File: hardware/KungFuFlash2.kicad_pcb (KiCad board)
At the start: 2 copper layers, 60.6 x 62 mm, 53 parts, among them J1 SWD, J2 USB_B_Micro, J3 Wifi, Q1 BC817, SW1 Reset, SW2 Menu, SW3 Special, U1 C64-Exp-Port, U2 AMS1117-3.3, U3 STM32H7B0VBTx, Y1 25MHz

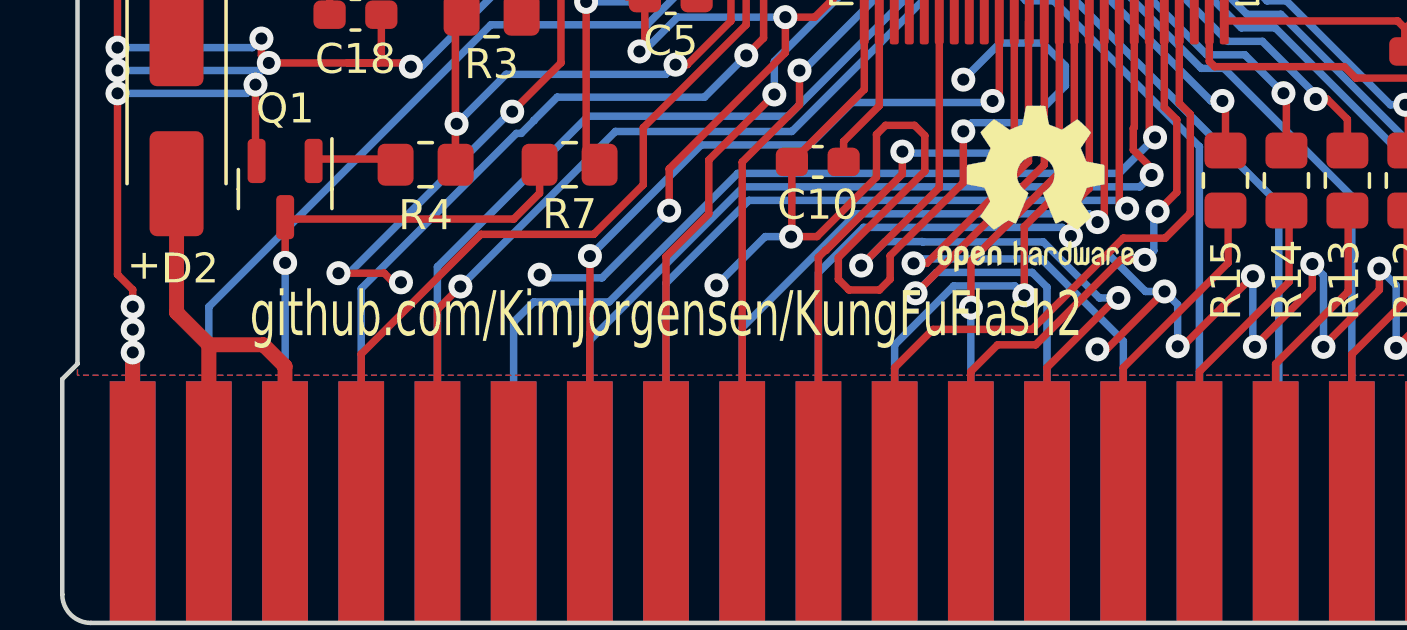
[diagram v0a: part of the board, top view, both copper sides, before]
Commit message: Move to Codeberg
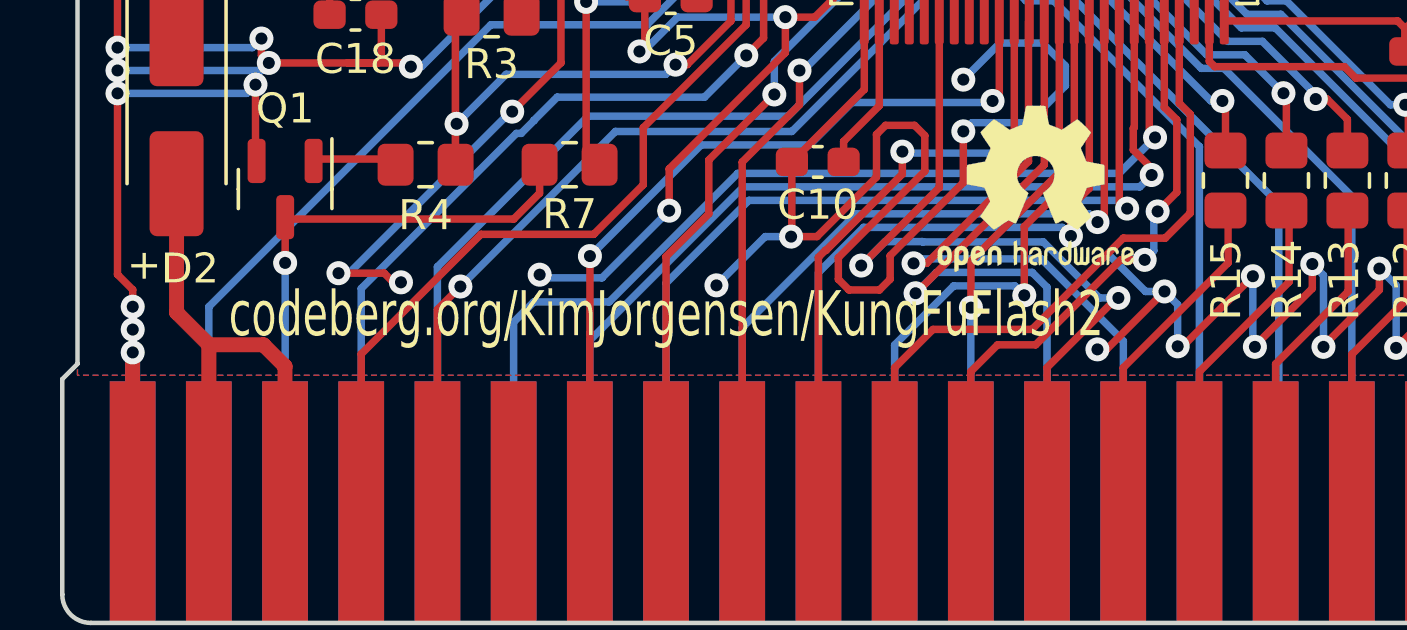
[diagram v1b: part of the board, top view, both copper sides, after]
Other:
- board text added: "codeberg.org/KimJorgensen/KungFuFlash2"
- board text removed: "github.com/KimJorgensen/KungFuFlash2"
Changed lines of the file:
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@@
   (gr_line (start 133.9215 122.047) (end 133.4135 121.539)
     (stroke (width 0.15) (type solid)) (layer "Edge.Cuts"))
-  (gr_text "github.com/KimJorgensen/KungFuFlash2" (at 96.012 119.888) (layer "F.SilkS")
+  (gr_text "codeberg.org/KimJorgensen/KungFuFlash2" (at 96.012 119.888) (layer "F.SilkS")
     (effects (font (size 1.5 1) (thickness 0.25)))
   )
